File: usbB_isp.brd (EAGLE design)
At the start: 100 x 80 mm, 12 parts, among them IC1 788TV, IC2 TINY13-20PU, X1 PN61729-S

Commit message: routing
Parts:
- moved SV2 21.0 mm to (68.8, 11.4)
- moved C3 17.0 mm to (61.3, 11.8), turned to 90 degrees
- moved R1 16.1 mm to (52.0, 17.6)
- moved IC2 15.1 mm to (52.6, 10.2)
- moved R2 10.8 mm to (40.0, 16.0)
- moved R4 10.8 mm to (40.0, 19.0)
- moved R3 8.25 mm to (41.0, 9.00), turned to 315 degrees
- moved C2 6.00 mm to (9.75, 5.08)
- moved LED1 5.83 mm to (30.0, 13.0)
- moved X1 5.10 mm to (4.08, 13.9)
- moved IC1 2.00 mm to (17.0, 19.6)
- moved C1 1.00 mm to (18.8, 11.7), turned to 180 degrees
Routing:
- net GND: track 0.00 -> 160.4 mm
- net VCC: track 0.00 -> 69.4 mm
- net MISO: track 0.00 -> 52.4 mm
- net N$9: track 0.00 -> 46.3 mm
- net _RESET: track 0.00 -> 36.6 mm
- net N$10: track 0.00 -> 24.8 mm
- net N$3: track 0.00 -> 20.2 mm
- net N$1: track 0.00 -> 17.9 mm
- net N$7: track 0.00 -> 16.1 mm
- net SCK: track 0.00 -> 14.6 mm
- net N$6: track 0.00 -> 10.7 mm
- net N$8: track 0.00 -> 6.11 mm
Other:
- board text added: "Netz39"

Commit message: fixing some errors i.e. width
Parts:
- moved C2 0.89 mm to (10.5, 4.68)
- moved X1 0.76 mm to (4.38, 13.2)
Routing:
- net GND: track 160.4 -> 163.9 mm
- net N$1: track 17.9 -> 18.7 mm
- added copper zone on layer 16, net GND
- removed copper zone on layer 16, net N$2

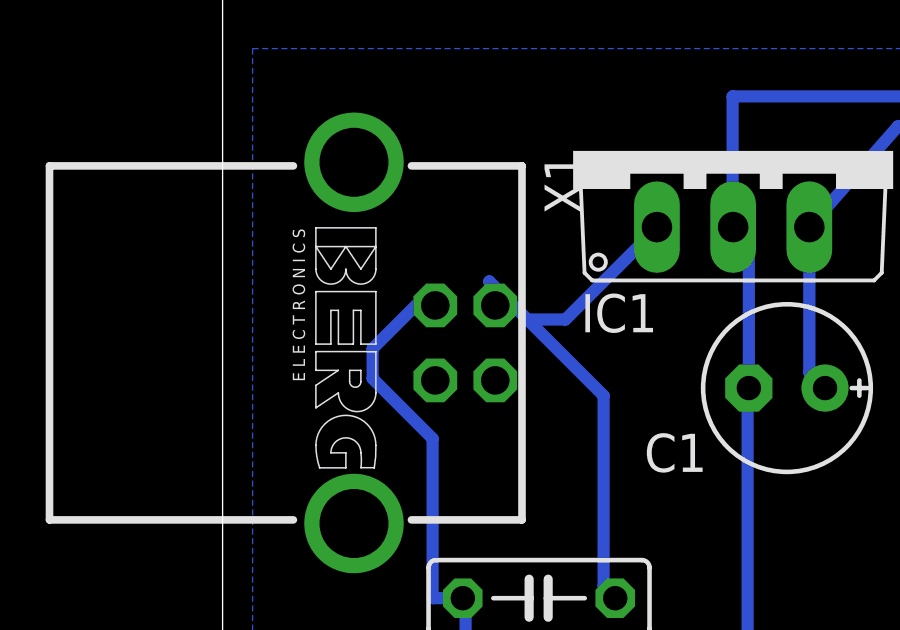
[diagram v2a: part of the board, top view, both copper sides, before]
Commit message: fixing mass pin
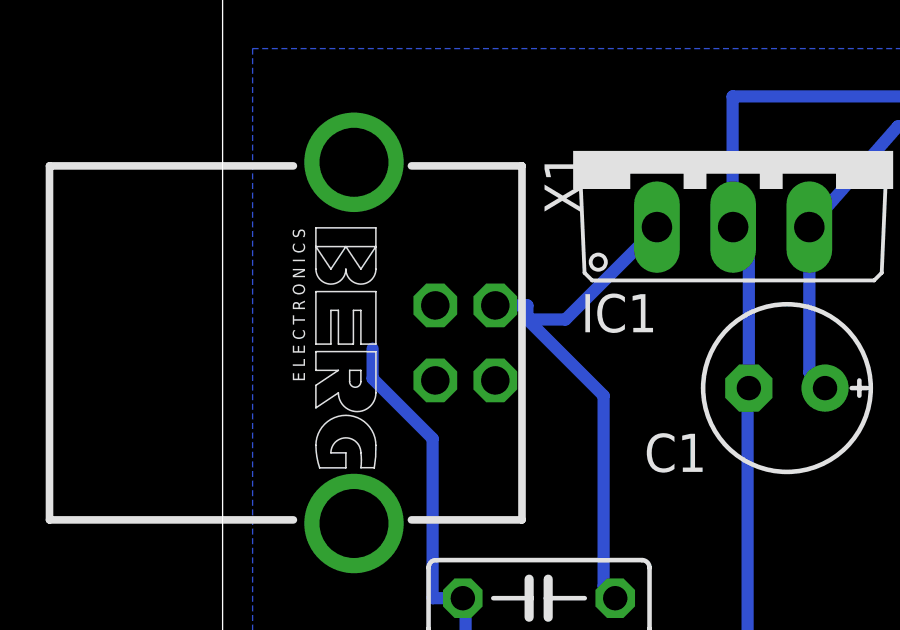
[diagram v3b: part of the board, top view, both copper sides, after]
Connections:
- net GND: now also X1.4, X1.S1; no longer X1.3
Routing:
- net GND: track 163.9 -> 160.9 mm
- net N$1: track 18.7 -> 17.6 mm
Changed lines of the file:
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@@
 <setting verticaltext="up"/>
 </settings>
-<grid distance="39.3700787" unitdist="mil" unit="mil" style="lines" multiple="1" display="no" altdistance="0.5" altunitdist="mm" altunit="mm"/>
+<grid distance="1" unitdist="mm" unit="mm" style="lines" multiple="1" display="no" altdistance="0.5" altunitdist="mm" altunit="mm"/>
 <layers>
-<layer number="1" name="Top" color="4" fill="1" visible="no" active="yes"/>
+<layer number="1" name="Top" color="4" fill="1" visible="yes" active="yes"/>
 <layer number="16" name="Bottom" color="1" fill="1" visible="yes" active="yes"/>
 <layer number="17" name="Pads" color="2" fill="1" visible="yes" active="yes"/>
 <layer number="18" name="Vias" color="2" fill="1" visible="yes" active="yes"/>
-<layer number="19" name="Unrouted" color="6" fill="1" visible="no" active="yes"/>
-<layer number="20" name="Dimension" color="15" fill="1" visible="no" active="yes"/>
-<layer number="21" name="tPlace" color="7" fill="1" visible="no" active="yes"/>
-<layer number="22" name="bPlace" color="7" fill="1" visible="no" active="yes"/>
-<layer number="23" name="tOrigins" color="15" fill="1" visible="no" active="yes"/>
-<layer number="24" name="bOrigins" color="15" fill="1" visible="no" active="yes"/>
-<layer number="25" name="tNames" color="7" fill="1" visible="no" active="yes"/>
-<layer number="26" name="bNames" color="7" fill="1" visible="no" active="yes"/>
-<layer number="27" name="tValues" color="7" fill="1" visible="no" active="yes"/>
-<layer number="28" name="bValues" color="7" fill="1" visible="no" active="yes"/>
-<layer number="29" name="tStop" color="7" fill="3" visible="no" active="yes"/>
-<layer number="30" name="bStop" color="7" fill="6" visible="no" active="yes"/>
-<layer number="31" name="tCream" color="7" fill="4" visible="no" active="yes"/>
-<layer number="32" name="bCream" color="7" fill="5" visible="no" active="yes"/>
-<layer number="33" name="tFinish" color="6" fill="3" visible="no" active="yes"/>
-<layer number="34" name="bFinish" color="6" fill="6" visible="no" active="yes"/>
-<layer number="35" name="tGlue" color="7" fill="4" visible="no" active="yes"/>
-<layer number="36" name="bGlue" color="7" fill="5" visible="no" active="yes"/>
-<layer number="37" name="tTest" color="7" fill="1" visible="no" active="yes"/>
-<layer number="38" name="bTest" color="7" fill="1" visible="no" active="yes"/>
-<layer number="39" name="tKeepout" color="4" fill="11" visible="no" active="yes"/>
-<layer number="40" name="bKeepout" color="1" fill="11" visible="no" active="yes"/>
-<layer number="41" name="tRestrict" color="4" fill="10" visible="no" active="yes"/>
-<layer number="42" name="bRestrict" color="1" fill="10" visible="no" active="yes"/>
-<layer number="43" name="vRestrict" color="2" fill="10" visible="no" active="yes"/>
-<layer number="44" name="Drills" color="7" fill="1" visible="no" active="yes"/>
-<layer number="45" name="Holes" color="7" fill="1" visible="no" active="yes"/>
-<layer number="46" name="Milling" color="3" fill="1" visible="no" active="yes"/>
-<layer number="47" name="Measures" color="7" fill="1" visible="no" active="yes"/>
-<layer number="48" name="Document" color="7" fill="1" visible="no" active="yes"/>
-<layer number="49" name="Reference" color="7" fill="1" visible="no" active="yes"/>
-<layer number="51" name="tDocu" color="7" fill="1" visible="no" active="yes"/>
-<layer number="52" name="bDocu" color="7" fill="1" visible="no" active="yes"/>
+<layer number="19" name="Unrouted" color="6" fill="1" visible="yes" active="yes"/>
+<layer number="20" name="Dimension" color="15" fill="1" visible="yes" active="yes"/>
+<layer number="21" name="tPlace" color="7" fill="1" visible="yes" active="yes"/>
+<layer number="22" name="bPlace" color="7" fill="1" visible="yes" active="yes"/>
+<layer number="23" name="tOrigins" color="15" fill="1" visible="yes" active="yes"/>
+<layer number="24" name="bOrigins" color="15" fill="1" visible="yes" active="yes"/>
+<layer number="25" name="tNames" color="7" fill="1" visible="yes" active="yes"/>
+<layer number="26" name="bNames" color="7" fill="1" visible="yes" active="yes"/>
+<layer number="27" name="tValues" color="7" fill="1" visible="yes" active="yes"/>
+<layer number="28" name="bValues" color="7" fill="1" visible="yes" active="yes"/>
+<layer number="29" name="tStop" color="7" fill="3" visible="yes" active="yes"/>
+<layer number="30" name="bStop" color="7" fill="6" visible="yes" active="yes"/>
+<layer number="31" name="tCream" color="7" fill="4" visible="yes" active="yes"/>
+<layer number="32" name="bCream" color="7" fill="5" visible="yes" active="yes"/>
+<layer number="33" name="tFinish" color="6" fill="3" visible="yes" active="yes"/>
+<layer number="34" name="bFinish" color="6" fill="6" visible="yes" active="yes"/>
+<layer number="35" name="tGlue" color="7" fill="4" visible="yes" active="yes"/>
+<layer number="36" name="bGlue" color="7" fill="5" visible="yes" active="yes"/>
+<layer number="37" name="tTest" color="7" fill="1" visible="yes" active="yes"/>
+<layer number="38" name="bTest" color="7" fill="1" visible="yes" active="yes"/>
+<layer number="39" name="tKeepout" color="4" fill="11" visible="yes" active="yes"/>
+<layer number="40" name="bKeepout" color="1" fill="11" visible="yes" active="yes"/>
+<layer number="41" name="tRestrict" color="4" fill="10" visible="yes" active="yes"/>
+<layer number="42" name="bRestrict" color="1" fill="10" visible="yes" active="yes"/>
+<layer number="43" name="vRestrict" color="2" fill="10" visible="yes" active="yes"/>
+<layer number="44" name="Drills" color="7" fill="1" visible="yes" active="yes"/>
+<layer number="45" name="Holes" color="7" fill="1" visible="yes" active="yes"/>
+<layer number="46" name="Milling" color="3" fill="1" visible="yes" active="yes"/>
+<layer number="47" name="Measures" color="7" fill="1" visible="yes" active="yes"/>
+<layer number="48" name="Document" color="7" fill="1" visible="yes" active="yes"/>
+<layer number="49" name="Reference" color="7" fill="1" visible="yes" active="yes"/>
+<layer number="51" name="tDocu" color="7" fill="1" visible="yes" active="yes"/>
+<layer number="52" name="bDocu" color="7" fill="1" visible="yes" active="yes"/>
 <layer number="91" name="Nets" color="2" fill="1" visible="no" active="no"/>
 <layer number="92" name="Busses" color="1" fill="1" visible="no" active="no"/>
@@
 <contactref element="X1" pad="2"/>
 <wire x1="12.7" y1="11.43" x2="12.7" y2="5.08" width="0.4064" layer="16"/>
-<wire x1="8.89" y1="15.24" x2="10.16" y2="13.97" width="0.4064" layer="16"/>
 <wire x1="10.16" y1="13.97" x2="12.7" y2="11.43" width="0.4064" layer="16"/>
 <wire x1="12.7" y1="5.08" x2="13.088" y2="4.68" width="0.4064" layer="16"/>
-<wire x1="8.89" y1="15.24" x2="9.09" y2="14.44" width="0.4064" layer="16"/>
 <wire x1="11.43" y1="13.97" x2="13.97" y2="16.51" width="0.4064" layer="16"/>
 <wire x1="10.16" y1="13.97" x2="11.43" y2="13.97" width="0.4064" layer="16"/>
 <wire x1="13.97" y1="16.51" x2="14.478" y2="17.05" width="0.4064" layer="16"/>
+<wire x1="9.09" y1="14.44" x2="10.16" y2="14.44" width="0.4064" layer="16"/>
+<wire x1="10.16" y1="14.44" x2="10.16" y2="13.97" width="0.4064" layer="16"/>
 </signal>
 <signal name="GND">
@@
 <contactref element="R3" pad="2"/>
 <contactref element="R4" pad="2"/>
-<contactref element="X1" pad="3"/>
 <contactref element="SV2" pad="6"/>
 <wire x1="69.297" y1="12.6508" x2="67.9762" y2="13.9954" width="0.4064" layer="16"/>
@@
 <wire x1="17.5" y1="3.5" x2="17.5" y2="11.642" width="0.4064" layer="16"/>
 <wire x1="17.5" y1="11.642" x2="17.542" y2="11.684" width="0.4064" layer="16"/>
-<wire x1="7.09" y1="14.44" x2="6.79" y2="14.79" width="0.4064" layer="16"/>
-<wire x1="6.79" y1="14.79" x2="5" y2="13" width="0.4064" layer="16"/>
 <wire x1="5" y1="13" x2="5" y2="12" width="0.4064" layer="16"/>
 <wire x1="5" y1="12" x2="7" y2="10" width="0.4064" layer="16"/>
@@
 <wire x1="8.1" y1="4.5" x2="8.1" y2="3" width="0.4064" layer="16"/>
 <wire x1="8.1" y1="3" x2="17" y2="3" width="0.4064" layer="16"/>
-<polygon width="0.4064" layer="16" isolate="0.5842">
+<polygon width="0.4064" layer="16" isolate="0.5842" thermals="no">
 <vertex x="1" y="23"/>
 <vertex x="75" y="23"/>
@@
 <vertex x="1" y="2"/>
 </polygon>
+<contactref element="X1" pad="4"/>
+<contactref element="X1" pad="S1"/>
 </signal>
 <signal name="VCC">
